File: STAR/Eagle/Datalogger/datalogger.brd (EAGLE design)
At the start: 26.4 x 55.9 mm, 7 parts, among them J1 J30J-25

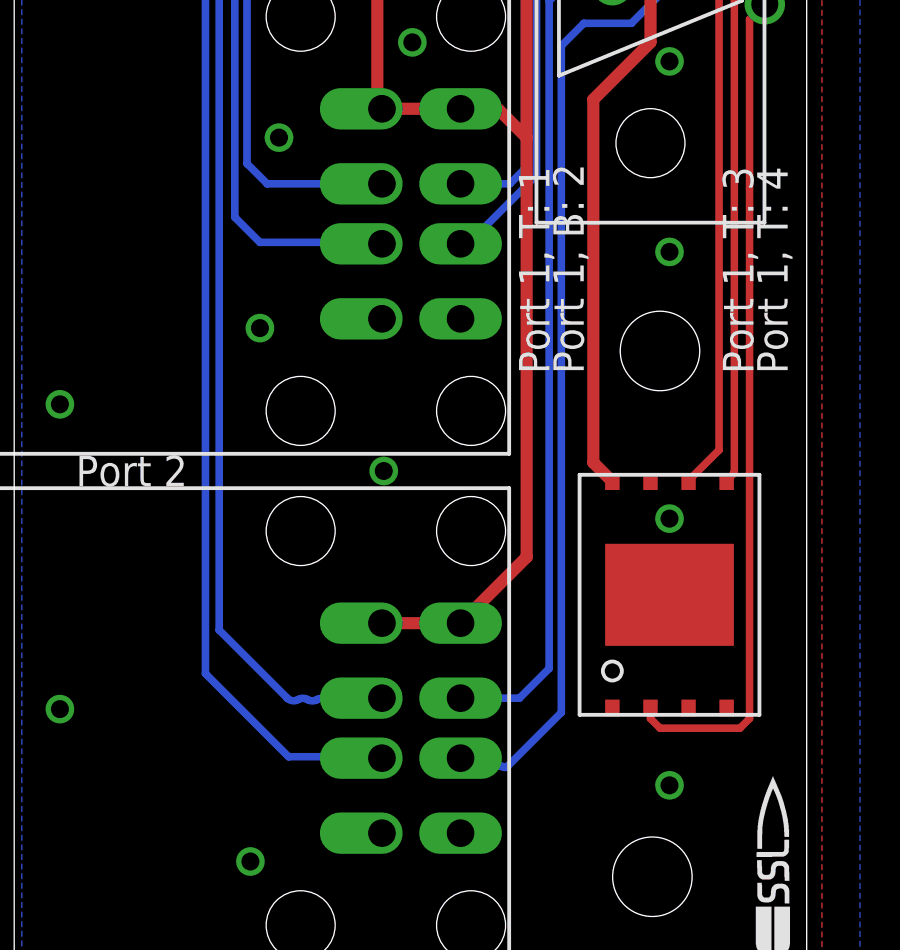
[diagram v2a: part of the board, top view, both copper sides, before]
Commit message: fixed datalogger USB port
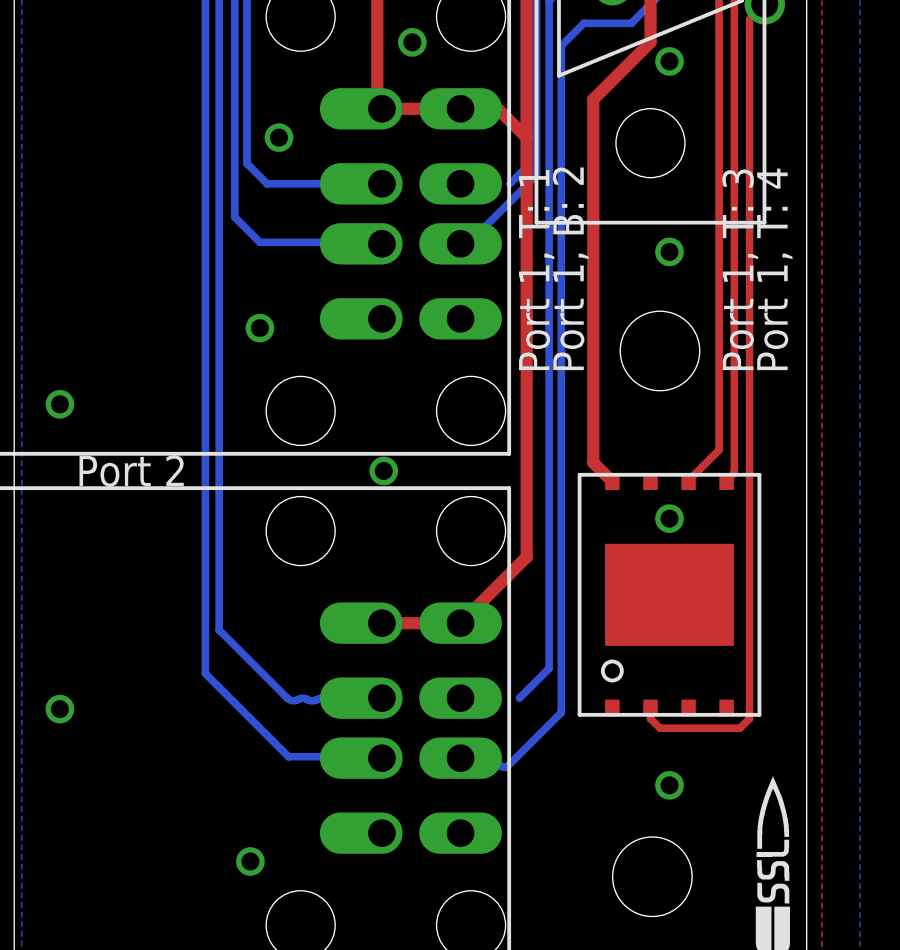
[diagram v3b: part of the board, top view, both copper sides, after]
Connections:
- net DATA1_N: now also U$2.DATA+1; no longer U$2.DATA-1
- net DATA1_P: now also U$2.DATA-1; no longer U$2.DATA+1
- net DATA2_N: now also U$2.DATA+2; no longer U$2.DATA-2
- net DATA2_P: now also U$2.DATA-2; no longer U$2.DATA+2
- net DATA3_N: now also U$3.DATA+1; no longer U$3.DATA-1
- net DATA3_P: now also U$3.DATA-1; no longer U$3.DATA+1
- net DATA4_N: now also U$3.DATA+2; no longer U$3.DATA-2
- net DATA4_P: now also U$3.DATA-2; no longer U$3.DATA+2
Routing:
- net DATA1_P: track 31.8 -> 29.8 mm
- net DATA3_P: track 13.4 -> 11.8 mm
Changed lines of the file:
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@@
 </signal>
 <signal name="DATA1_P">
-<contactref element="U$2" pad="DATA+1"/>
 <contactref element="J1" pad="4"/>
-<wire x1="3.88763125" y1="-4.715" x2="1.925" y2="-4.715" width="0.254" layer="16"/>
 <wire x1="4.8768" y1="-3.72583125" x2="3.88763125" y2="-4.715" width="0.254" layer="16"/>
 <wire x1="4.8768" y1="-3.72583125" x2="4.8768" y2="18.5293" width="0.254" layer="16"/>
@@
 <wire x1="9.2075" y1="22.225" x2="7.3025" y2="20.32" width="0.254" layer="16"/>
 <wire x1="9.2075" y1="22.225" x2="9.525" y2="22.225" width="0.254" layer="16"/>
+<contactref element="U$2" pad="DATA-1"/>
+<wire x1="3.88763125" y1="-4.715" x2="1.925" y2="-6.715" width="0" layer="19" extent="16-16"/>
 </signal>
 <signal name="DATA1_N">
-<contactref element="U$2" pad="DATA-1"/>
 <contactref element="J1" pad="2"/>
 <wire x1="5.2832" y1="-5.1943" x2="5.2832" y2="17.0307" width="0.254" layer="16"/>
@@
 <wire x1="3.4925" y1="-6.985" x2="3.302" y2="-6.985" width="0.254" layer="16" curve="-90"/>
 <wire x1="3.302" y1="-6.985" x2="2.195" y2="-6.985" width="0.254" layer="16"/>
-<wire x1="2.195" y1="-6.985" x2="1.925" y2="-6.715" width="0.254" layer="16"/>
+<contactref element="U$2" pad="DATA+1"/>
+<wire x1="2.195" y1="-6.985" x2="1.925" y2="-4.715" width="0" layer="19" extent="16-16"/>
 </signal>
 <signal name="DATA2_P">
-<contactref element="U$2" pad="DATA+2"/>
 <contactref element="J1" pad="22"/>
 <wire x1="-3.85170625" y1="-4.715" x2="-6.1214" y2="-2.44530625" width="0.254" layer="16"/>
@@
 <wire x1="-2.8575" y1="-4.7625" x2="-2.54" y2="-4.7625" width="0.254" layer="16" curve="-59.868965"/>
 <wire x1="-2.54" y1="-4.7625" x2="-0.7425" y2="-4.7625" width="0.254" layer="16"/>
-<wire x1="-0.7425" y1="-4.7625" x2="-0.695" y2="-4.715" width="0.254" layer="16"/>
+<contactref element="U$2" pad="DATA-2"/>
+<wire x1="-0.7425" y1="-4.7625" x2="-0.695" y2="-6.715" width="0" layer="19" extent="16-16"/>
 </signal>
 <signal name="DATA2_N">
-<contactref element="U$2" pad="DATA-2"/>
 <contactref element="J1" pad="23"/>
 <wire x1="-6.5786" y1="29.30469375" x2="-5.17469375" y2="30.7086" width="0.254" layer="16"/>
@@
 <wire x1="-6.5786" y1="-3.8989" x2="-3.81" y2="-6.6675" width="0.254" layer="16"/>
 <wire x1="-3.81" y1="-6.6675" x2="-0.7425" y2="-6.6675" width="0.254" layer="16"/>
-<wire x1="-0.7425" y1="-6.6675" x2="-0.695" y2="-6.715" width="0.254" layer="16"/>
+<contactref element="U$2" pad="DATA+2"/>
+<wire x1="-0.695" y1="-4.715" x2="-0.7425" y2="-6.6675" width="0" layer="19" extent="16-16"/>
 </signal>
 <signal name="DATA3_P">
-<contactref element="U$3" pad="DATA+1"/>
 <contactref element="J1" pad="17"/>
 <wire x1="3.57013125" y1="12.43" x2="4.0513" y2="12.91116875" width="0.254" layer="16"/>
@@
 <wire x1="4.0513" y1="12.91116875" x2="4.0513" y2="18.8087" width="0.254" layer="16"/>
 <wire x1="2.8575" y1="20.0025" x2="4.0513" y2="18.8087" width="0.254" layer="16"/>
-<wire x1="3.57013125" y1="12.43" x2="1.925" y2="12.43" width="0.254" layer="16"/>
+<contactref element="U$3" pad="DATA-1"/>
+<wire x1="1.925" y1="10.43" x2="3.57013125" y2="12.43" width="0" layer="19" extent="16-16"/>
 </signal>
 <signal name="DATA3_N">
-<contactref element="U$3" pad="DATA-1"/>
 <contactref element="J1" pad="16"/>
 <wire x1="4.4577" y1="12.74283125" x2="4.4577" y2="18.7452" width="0.254" layer="16"/>
@@
 <wire x1="4.4577" y1="12.74283125" x2="4.445" y2="12.7" width="0.254" layer="16" curve="-33.03151"/>
 <wire x1="4.445" y1="12.7" x2="2.175" y2="10.43" width="0.254" layer="16"/>
-<wire x1="2.175" y1="10.43" x2="1.925" y2="10.43" width="0.254" layer="16" curve="-90"/>
+<contactref element="U$3" pad="DATA+1"/>
+<wire x1="1.925" y1="12.43" x2="2.175" y2="10.43" width="0" layer="19" extent="16-16"/>
 </signal>
 <signal name="DATA4_P">
-<contactref element="U$3" pad="DATA+2"/>
 <contactref element="J1" pad="20"/>
 <wire x1="-4.52263125" y1="12.43" x2="-5.1943" y2="13.10166875" width="0.254" layer="16"/>
@@
 <wire x1="-1.5875" y1="12.3825" x2="-1.27" y2="12.3825" width="0.254" layer="16" curve="-62.581327"/>
 <wire x1="-0.7425" y1="12.3825" x2="-1.27" y2="12.3825" width="0.254" layer="16"/>
-<wire x1="-0.695" y1="12.43" x2="-0.7425" y2="12.3825" width="0.254" layer="16"/>
 <wire x1="-2.5875" y1="12.43" x2="-4.52263125" y2="12.43" width="0.254" layer="16"/>
 <wire x1="-2.5875" y1="12.43" x2="-2.54" y2="12.3825" width="0.254" layer="16"/>
 <wire x1="-2.54" y1="12.3825" x2="-1.5875" y2="12.3825" width="0.254" layer="16"/>
+<contactref element="U$3" pad="DATA-2"/>
+<wire x1="-0.7425" y1="12.3825" x2="-0.695" y2="10.43" width="0" layer="19" extent="16-16"/>
 </signal>
 <signal name="DATA4_N">
-<contactref element="U$3" pad="DATA-2"/>
 <contactref element="J1" pad="21"/>
 <wire x1="-5.6007" y1="27.38916875" x2="-4.84666875" y2="28.1432" width="0.254" layer="16"/>
@@
 <wire x1="-5.6007" y1="11.3157" x2="-4.7625" y2="10.4775" width="0.254" layer="16"/>
 <wire x1="-0.7425" y1="10.4775" x2="-4.7625" y2="10.4775" width="0.254" layer="16"/>
-<wire x1="-0.7425" y1="10.4775" x2="-0.695" y2="10.43" width="0.254" layer="16"/>
 <wire x1="-5.6007" y1="11.3157" x2="-5.6007" y2="27.38916875" width="0.254" layer="16"/>
+<contactref element="U$3" pad="DATA+2"/>
+<wire x1="-0.7425" y1="10.4775" x2="-0.695" y2="12.43" width="0" layer="19" extent="16-16"/>
 </signal>
 <signal name="SCK_FLASH">

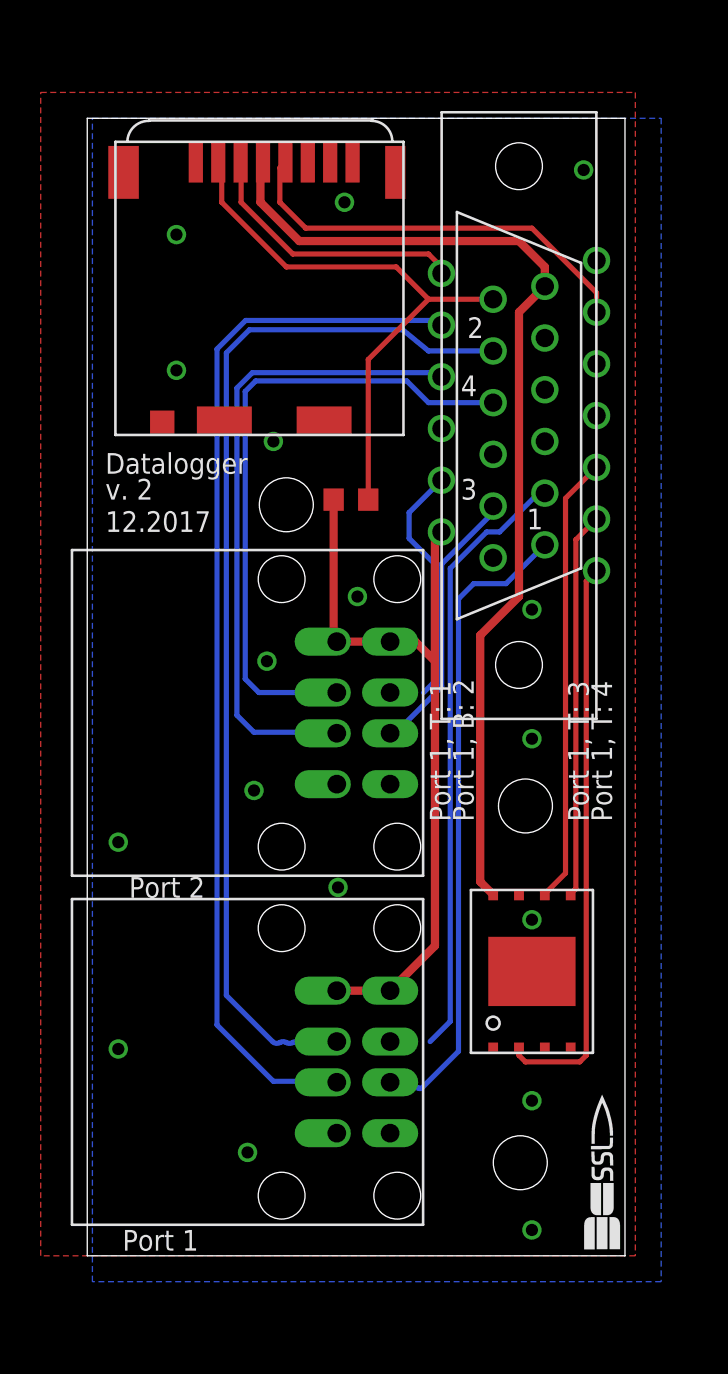
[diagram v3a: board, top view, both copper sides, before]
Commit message: datalogger differential pairs
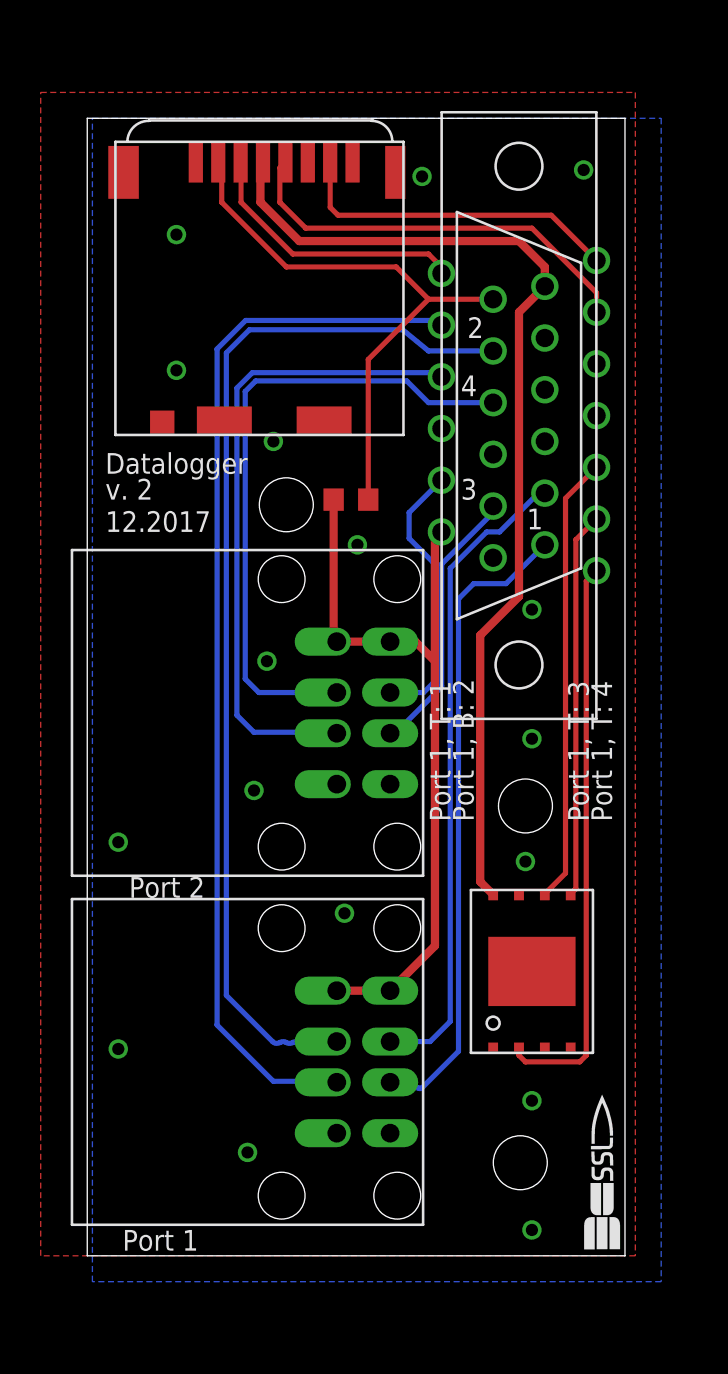
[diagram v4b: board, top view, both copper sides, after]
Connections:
- net DATA1_N: now also U$2.DATA-1; no longer U$2.DATA+1
- net DATA1_P: now also U$2.DATA+1; no longer U$2.DATA-1
- net DATA2_N: now also U$2.DATA-2; no longer U$2.DATA+2
- net DATA2_P: now also U$2.DATA+2; no longer U$2.DATA-2
- net DATA3_N: now also U$3.DATA-1; no longer U$3.DATA+1
- net DATA3_P: now also U$3.DATA+1; no longer U$3.DATA-1
- net DATA4_N: now also U$3.DATA-2; no longer U$3.DATA+2
- net DATA4_P: now also U$3.DATA+2; no longer U$3.DATA-2
- net GND: no longer J1.13
- net MOSI_STAR: now also J1.13
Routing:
- net MOSI_STAR: track 0.00 -> 16.4 mm
- net DATA1_P: track 29.8 -> 31.8 mm
- net DATA3_P: track 11.8 -> 13.4 mm
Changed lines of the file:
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@@
 <setting verticaltext="up"/>
 </settings>
-<grid distance="0.05" unitdist="inch" unit="inch" style="lines" multiple="1" display="no" altdistance="0.0125" altunitdist="inch" altunit="inch"/>
+<grid distance="0.05" unitdist="inch" unit="inch" style="lines" multiple="1" display="no" altdistance="0.0025" altunitdist="inch" altunit="inch"/>
 <layers>
 <layer number="1" name="Top" color="4" fill="1" visible="yes" active="yes"/>
@@
 <contactref element="U$5" pad="P$PAD"/>
 <contactref element="U$5" pad="P$1"/>
-<contactref element="J1" pad="13"/>
 <via x="-11.43" y="-5.08" extent="1-16" drill="0.6"/>
 <via x="-5.08" y="-10.16" extent="1-16" drill="0.6"/>
 <via x="8.89" y="-13.97" extent="1-16" drill="0.6"/>
 <via x="8.89" y="-7.62" extent="1-16" drill="0.6"/>
-<via x="8.89" y="1.27" extent="1-16" drill="0.6"/>
+<via x="8.5725" y="4.1275" extent="1-16" drill="0.6"/>
 <via x="8.89" y="10.16" extent="1-16" drill="0.6"/>
 <via x="-11.43" y="5.08" extent="1-16" drill="0.6"/>
 <via x="-4.7625" y="7.62" extent="1-16" drill="0.6"/>
-<via x="-0.635" y="2.8575" extent="1-16" drill="0.6"/>
+<via x="-0.3175" y="1.5875" extent="1-16" drill="0.6"/>
 <via x="-4.1275" y="13.97" extent="1-16" drill="0.6"/>
-<via x="0.3175" y="17.145" extent="1-16" drill="0.6"/>
+<via x="0.3175" y="19.685" extent="1-16" drill="0.6"/>
 <via x="8.89" y="16.51" extent="1-16" drill="0.6"/>
 <via x="11.43" y="38.1" extent="1-16" drill="0.6"/>
 <via x="-8.5725" y="34.925" extent="1-16" drill="0.6"/>
 <via x="-8.5725" y="28.2575" extent="1-16" drill="0.6"/>
-<via x="-0.3175" y="36.5125" extent="1-16" drill="0.6"/>
+<via x="3.4925" y="37.7825" extent="1-16" drill="0.6"/>
 <polygon width="0.4064" layer="16">
 <vertex x="-12.7" y="40.64"/>
@@
 <signal name="MOSI_STAR">
 <contactref element="U$1" pad="DAT0"/>
+<contactref element="J1" pad="13"/>
+<wire x1="-1.02" y1="38.4825" x2="-1.02" y2="36.2625" width="0.254" layer="1"/>
+<wire x1="-1.02" y1="36.2625" x2="-0.635" y2="35.8775" width="0.254" layer="1"/>
+<wire x1="-0.635" y1="35.8775" x2="9.8425" y2="35.8775" width="0.254" layer="1"/>
+<wire x1="9.8425" y1="35.8775" x2="12.065" y2="33.655" width="0.254" layer="1"/>
 </signal>
 <signal name="SCK_STAR">
@@
 <contactref element="J1" pad="4"/>
 <wire x1="4.8768" y1="-3.72583125" x2="3.88763125" y2="-4.715" width="0.254" layer="16"/>
-<wire x1="4.8768" y1="-3.72583125" x2="4.8768" y2="18.5293" width="0.254" layer="16"/>
+<wire x1="4.8768" y1="18.5293" x2="4.8768" y2="-3.72583125" width="0.254" layer="16"/>
 <wire x1="6.6675" y1="20.32" x2="4.8768" y2="18.5293" width="0.254" layer="16"/>
 <wire x1="6.6675" y1="20.32" x2="7.3025" y2="20.32" width="0.254" layer="16"/>
 <wire x1="9.2075" y1="22.225" x2="7.3025" y2="20.32" width="0.254" layer="16"/>
 <wire x1="9.2075" y1="22.225" x2="9.525" y2="22.225" width="0.254" layer="16"/>
-<contactref element="U$2" pad="DATA-1"/>
-<wire x1="3.88763125" y1="-4.715" x2="1.925" y2="-6.715" width="0" layer="19" extent="16-16"/>
+<contactref element="U$2" pad="DATA+1"/>
+<wire x1="3.88763125" y1="-4.715" x2="1.925" y2="-4.715" width="0.254" layer="16"/>
 </signal>
 <signal name="DATA1_N">
 <contactref element="J1" pad="2"/>
-<wire x1="5.2832" y1="-5.1943" x2="5.2832" y2="17.0307" width="0.254" layer="16"/>
+<wire x1="5.2832" y1="17.0307" x2="5.2832" y2="-5.1943" width="0.254" layer="16"/>
 <wire x1="6.0325" y1="17.78" x2="5.2832" y2="17.0307" width="0.254" layer="16"/>
 <wire x1="6.0325" y1="17.78" x2="7.62" y2="17.78" width="0.254" layer="16"/>
@@
 <wire x1="3.4925" y1="-6.985" x2="3.302" y2="-6.985" width="0.254" layer="16" curve="-90"/>
 <wire x1="3.302" y1="-6.985" x2="2.195" y2="-6.985" width="0.254" layer="16"/>
-<contactref element="U$2" pad="DATA+1"/>
-<wire x1="2.195" y1="-6.985" x2="1.925" y2="-4.715" width="0" layer="19" extent="16-16"/>
+<contactref element="U$2" pad="DATA-1"/>
+<wire x1="2.195" y1="-6.985" x2="1.925" y2="-6.715" width="0.254" layer="16"/>
 </signal>
 <signal name="DATA2_P">
@@
 <wire x1="-3.175" y1="-4.7625" x2="-2.8575" y2="-4.7625" width="0.254" layer="16" curve="59.868965"/>
 <wire x1="-2.8575" y1="-4.7625" x2="-2.54" y2="-4.7625" width="0.254" layer="16" curve="-59.868965"/>
+<contactref element="U$2" pad="DATA+2"/>
 <wire x1="-2.54" y1="-4.7625" x2="-0.7425" y2="-4.7625" width="0.254" layer="16"/>
-<contactref element="U$2" pad="DATA-2"/>
-<wire x1="-0.7425" y1="-4.7625" x2="-0.695" y2="-6.715" width="0" layer="19" extent="16-16"/>
+<wire x1="-0.7425" y1="-4.7625" x2="-0.695" y2="-4.715" width="0.254" layer="16"/>
 </signal>
 <signal name="DATA2_N">
@@
 <wire x1="-6.5786" y1="-3.8989" x2="-6.5786" y2="29.30469375" width="0.254" layer="16"/>
 <wire x1="-6.5786" y1="-3.8989" x2="-3.81" y2="-6.6675" width="0.254" layer="16"/>
+<contactref element="U$2" pad="DATA-2"/>
 <wire x1="-3.81" y1="-6.6675" x2="-0.7425" y2="-6.6675" width="0.254" layer="16"/>
-<contactref element="U$2" pad="DATA+2"/>
-<wire x1="-0.695" y1="-4.715" x2="-0.7425" y2="-6.6675" width="0" layer="19" extent="16-16"/>
+<wire x1="-0.7425" y1="-6.6675" x2="-0.695" y2="-6.715" width="0.254" layer="16"/>
 </signal>
 <signal name="DATA3_P">
@@
 <wire x1="4.0513" y1="12.91116875" x2="4.0513" y2="18.8087" width="0.254" layer="16"/>
 <wire x1="2.8575" y1="20.0025" x2="4.0513" y2="18.8087" width="0.254" layer="16"/>
-<contactref element="U$3" pad="DATA-1"/>
-<wire x1="1.925" y1="10.43" x2="3.57013125" y2="12.43" width="0" layer="19" extent="16-16"/>
+<contactref element="U$3" pad="DATA+1"/>
+<wire x1="3.57013125" y1="12.43" x2="1.925" y2="12.43" width="0.254" layer="16"/>
 </signal>
 <signal name="DATA3_N">
@@
 <wire x1="6.985" y1="21.2725" x2="6.985" y2="21.59" width="0.254" layer="16"/>
 <wire x1="4.4577" y1="12.74283125" x2="4.445" y2="12.7" width="0.254" layer="16" curve="-33.03151"/>
-<wire x1="4.445" y1="12.7" x2="2.175" y2="10.43" width="0.254" layer="16"/>
-<contactref element="U$3" pad="DATA+1"/>
-<wire x1="1.925" y1="12.43" x2="2.175" y2="10.43" width="0" layer="19" extent="16-16"/>
+<contactref element="U$3" pad="DATA-1"/>
+<wire x1="2.175" y1="10.43" x2="1.925" y2="10.43" width="0.254" layer="16"/>
+<wire x1="2.175" y1="10.43" x2="2.3495" y2="10.6045" width="0.254" layer="16" curve="90"/>
+<wire x1="2.3495" y1="10.6045" x2="4.445" y2="12.7" width="0.254" layer="16"/>
 </signal>
 <signal name="DATA4_P">
 <contactref element="J1" pad="20"/>
 <wire x1="-4.52263125" y1="12.43" x2="-5.1943" y2="13.10166875" width="0.254" layer="16"/>
-<wire x1="-5.1943" y1="13.10166875" x2="-5.1943" y2="27.22083125" width="0.254" layer="16"/>
+<wire x1="-5.1943" y1="27.22083125" x2="-5.1943" y2="13.10166875" width="0.254" layer="16"/>
 <wire x1="-5.1943" y1="27.22083125" x2="-4.67833125" y2="27.7368" width="0.254" layer="16"/>
 <wire x1="2.7432" y1="27.7368" x2="-4.67833125" y2="27.7368" width="0.254" layer="16"/>
@@
 <wire x1="3.81" y1="26.67" x2="6.985" y2="26.67" width="0.254" layer="16"/>
 <wire x1="-1.5875" y1="12.3825" x2="-1.27" y2="12.3825" width="0.254" layer="16" curve="-62.581327"/>
-<wire x1="-0.7425" y1="12.3825" x2="-1.27" y2="12.3825" width="0.254" layer="16"/>
 <wire x1="-2.5875" y1="12.43" x2="-4.52263125" y2="12.43" width="0.254" layer="16"/>
 <wire x1="-2.5875" y1="12.43" x2="-2.54" y2="12.3825" width="0.254" layer="16"/>
 <wire x1="-2.54" y1="12.3825" x2="-1.5875" y2="12.3825" width="0.254" layer="16"/>
-<contactref element="U$3" pad="DATA-2"/>
-<wire x1="-0.7425" y1="12.3825" x2="-0.695" y2="10.43" width="0" layer="19" extent="16-16"/>
+<contactref element="U$3" pad="DATA+2"/>
+<wire x1="-1.27" y1="12.3825" x2="-0.7425" y2="12.3825" width="0.254" layer="16"/>
+<wire x1="-0.7425" y1="12.3825" x2="-0.695" y2="12.43" width="0.254" layer="16"/>
 </signal>
 <signal name="DATA4_N">
@@
 <wire x1="4.2418" y1="28.1432" x2="4.445" y2="27.94" width="0.254" layer="16"/>
 <wire x1="-5.6007" y1="11.3157" x2="-4.7625" y2="10.4775" width="0.254" layer="16"/>
-<wire x1="-0.7425" y1="10.4775" x2="-4.7625" y2="10.4775" width="0.254" layer="16"/>
-<wire x1="-5.6007" y1="11.3157" x2="-5.6007" y2="27.38916875" width="0.254" layer="16"/>
-<contactref element="U$3" pad="DATA+2"/>
-<wire x1="-0.7425" y1="10.4775" x2="-0.695" y2="12.43" width="0" layer="19" extent="16-16"/>
+<wire x1="-5.6007" y1="27.38916875" x2="-5.6007" y2="11.3157" width="0.254" layer="16"/>
+<contactref element="U$3" pad="DATA-2"/>
+<wire x1="-4.7625" y1="10.4775" x2="-0.7425" y2="10.4775" width="0.254" layer="16"/>
+<wire x1="-0.7425" y1="10.4775" x2="-0.695" y2="10.43" width="0.254" layer="16"/>
 </signal>
 <signal name="SCK_FLASH">
